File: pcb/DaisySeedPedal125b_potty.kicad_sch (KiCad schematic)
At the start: 3 parts, among them J6 Conn_01x20_Socket, J7 Conn_01x20_Socket

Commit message: Lots of updates to Schematic and pcb design
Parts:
- added R28, R29: 4.7K, Resistor_SMD:R_0805_2012Metric, symbol Device:R
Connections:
- net I2C_SCL: now also R28.2
- net I2C_SDA: now also R29.2
- new net +5V: R28.1, R29.1

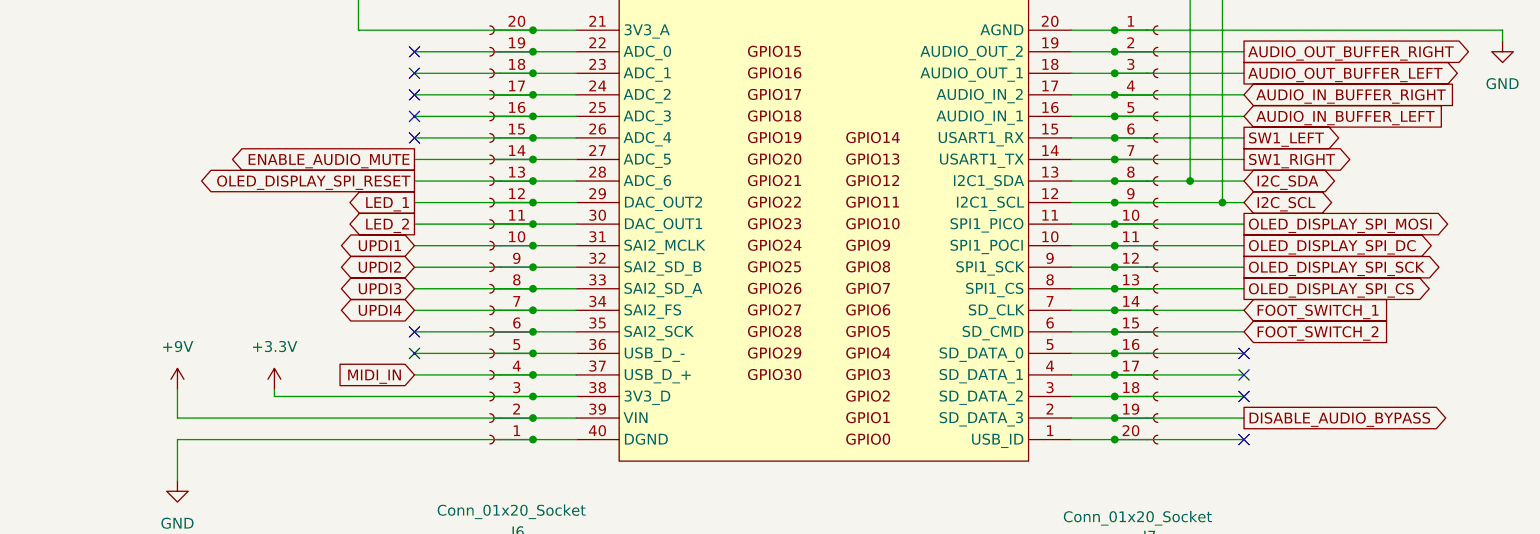
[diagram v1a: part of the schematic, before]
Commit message: Updated PCB, started laying tracks.
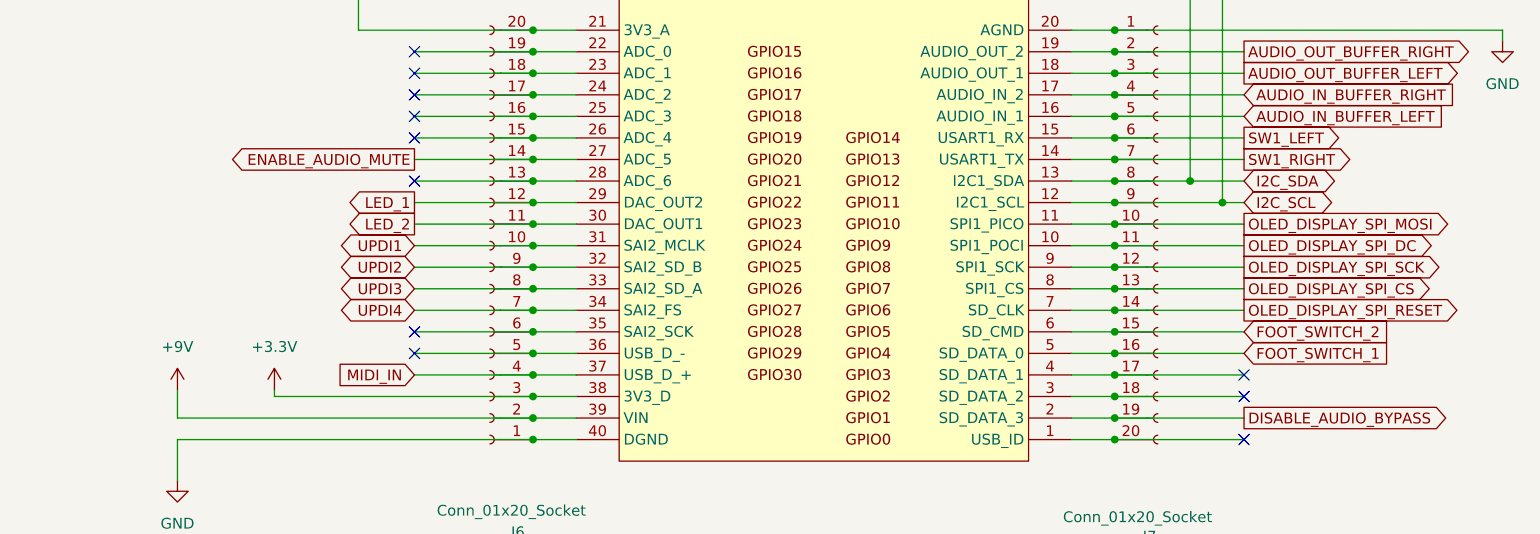
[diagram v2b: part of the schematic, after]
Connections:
- net FOOT_SWITCH_1: now also A1.5 (SD_DATA_0), J7.16 (Pin_16); no longer A1.7 (SD_CLK), J7.14 (Pin_14)
- net OLED_DISPLAY_SPI_RESET: now also A1.7 (SD_CLK), J7.14 (Pin_14); no longer A1.28 (ADC_6), J6.13 (Pin_13)
- new net: A1.28 (ADC_6), J6.13 (Pin_13)
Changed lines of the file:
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@@
 	)
 	(no_connect
-		(at 212.09 106.68)
+		(at 114.3 86.36)
 	)
 	(no_connect
@@
 	(global_label "OLED_DISPLAY_SPI_RESET"
 		(shape output)
-		(at 114.3 86.36 180)
-		(fields_autoplaced yes)
-		(effects
-			(font
-				(size 1.27 1.27)
-			)
-			(justify right)
-		)
-		(property "Intersheetrefs" "${INTERSHEET_REFS}"
-			(at 87.2454 86.36 0)
-			(effects
-				(font
-					(size 1.27 1.27)
-				)
-				(justify right)
+		(at 212.09 101.6 0)
+		(fields_autoplaced yes)
+		(effects
+			(font
+				(size 1.27 1.27)
+			)
+			(justify left)
+		)
+		(property "Intersheetrefs" "${INTERSHEET_REFS}"
+			(at 239.1446 101.6 0)
+			(effects
+				(font
+					(size 1.27 1.27)
+				)
+				(justify left)
 				(hide yes)
 			)
@@
 	(global_label "FOOT_SWITCH_1"
 		(shape input)
-		(at 212.09 101.6 0)
+		(at 212.09 106.68 0)
 		(fields_autoplaced yes)
 		(effects
@@
 		)
 		(property "Intersheetrefs" "${INTERSHEET_REFS}"
-			(at 229.1988 101.6794 0)
-			(effects
-				(font
+			(at 229.1988 106.7594 0)
+			(effects
+				(font

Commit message: Updates
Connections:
- net SW1_LEFT: no longer names the net of A1.15 (USART1_RX), J7.6 (Pin_6)
- net SW1_RIGHT: no longer names the net of A1.14 (USART1_TX), J7.7 (Pin_7)
- no-connect marks 11 -> 13
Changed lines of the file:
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@@
+	)
+	(no_connect
+		(at 212.09 83.82)
 	)
 	(no_connect
@@
 	(no_connect
 		(at 212.09 116.84)
+	)
+	(no_connect
+		(at 212.09 81.28)
 	)
 	(no_connect
@@
 		)
 	)
-	(global_label "SW1_RIGHT"
-		(shape output)
-		(at 212.09 83.82 0)
-		(fields_autoplaced yes)
-		(effects
-			(font
-				(size 1.27 1.27)
-			)
-			(justify left)
-		)
-		(property "Intersheetrefs" "${INTERSHEET_REFS}"
-			(at 225.3561 83.82 0)
-			(effects
-				(font
-					(size 1.27 1.27)
-				)
-				(justify left)
-				(hide yes)
-			)
-		)
-	)
 	(global_label "OLED_DISPLAY_SPI_CS"
 		(shape output)
@@
 			(effects
 				(font
-					(size 1.27 1.27)
-				)
-				(justify left)
-				(hide yes)
-			)
-		)
-	)
-	(global_label "SW1_LEFT"
-		(shape output)
-		(at 212.09 81.28 0)
-		(fields_autoplaced yes)
-		(effects
-			(font
-				(size 1.27 1.27)
-			)
-			(justify left)
-		)
-		(property "Intersheetrefs" "${INTERSHEET_REFS}"
-			(at 224.1465 81.28 0)
-			(effects
-				(font
